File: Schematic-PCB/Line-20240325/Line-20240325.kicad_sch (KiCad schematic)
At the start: 137 parts, among them J1 Conn_01x02_Pin, J2 Conn_01x04_Pin, J3 USB_C_Receptacle_USB2.0_16P, SW1 SW_Push, U33 ATmega2560-16A, U34 CH340E, Y1 16MHz

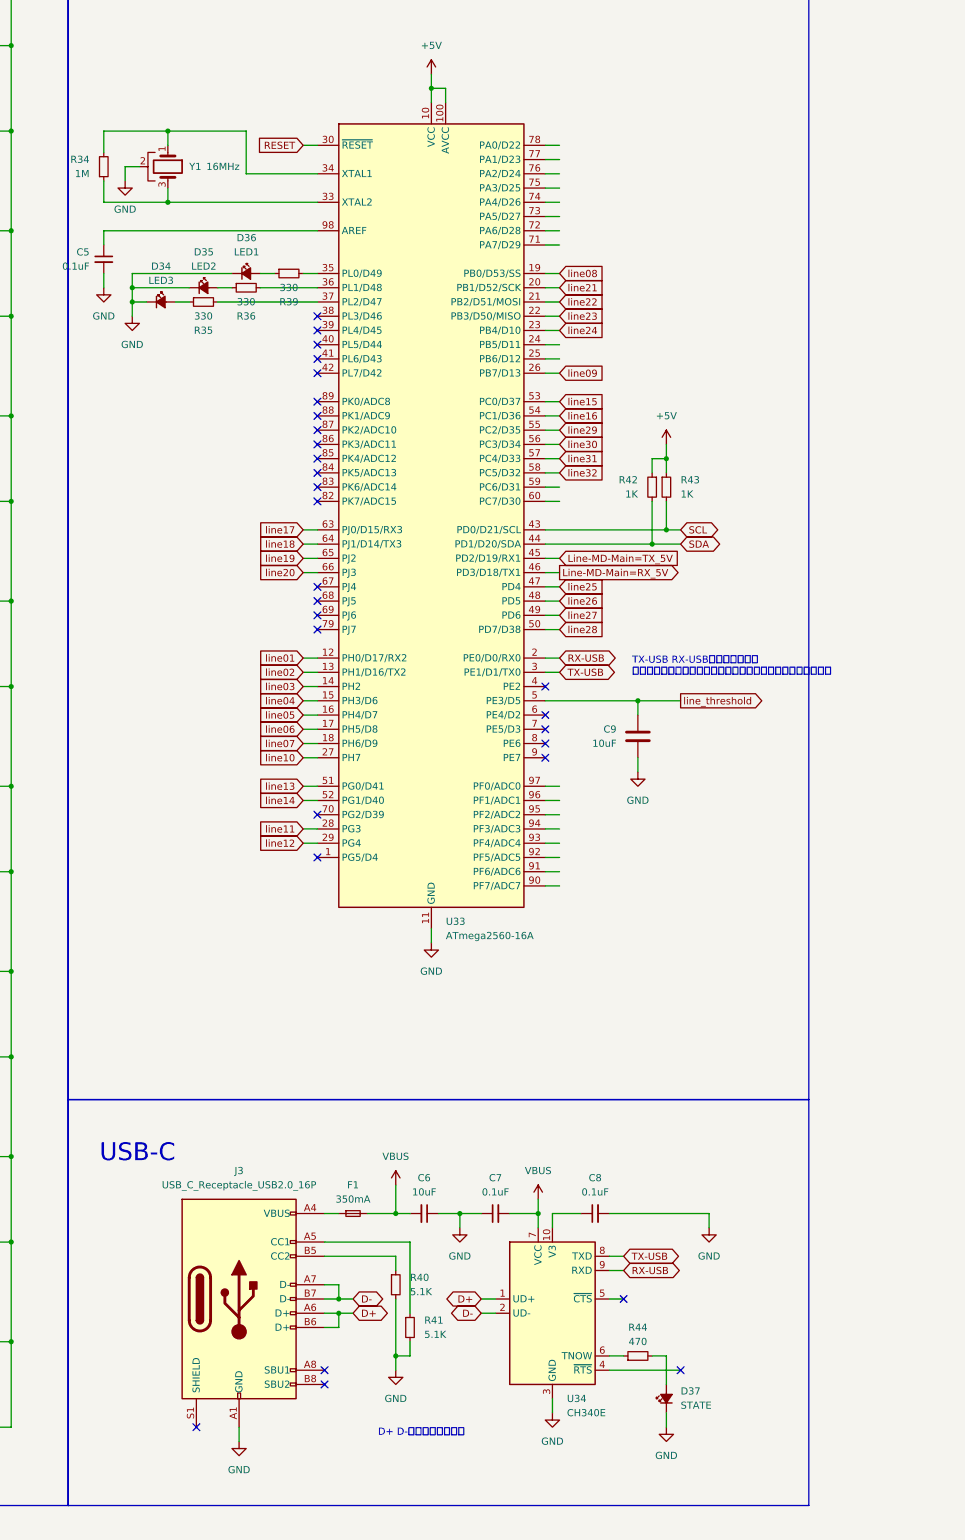
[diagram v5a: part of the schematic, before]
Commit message: ラインセンサ基板の回路図を見直した
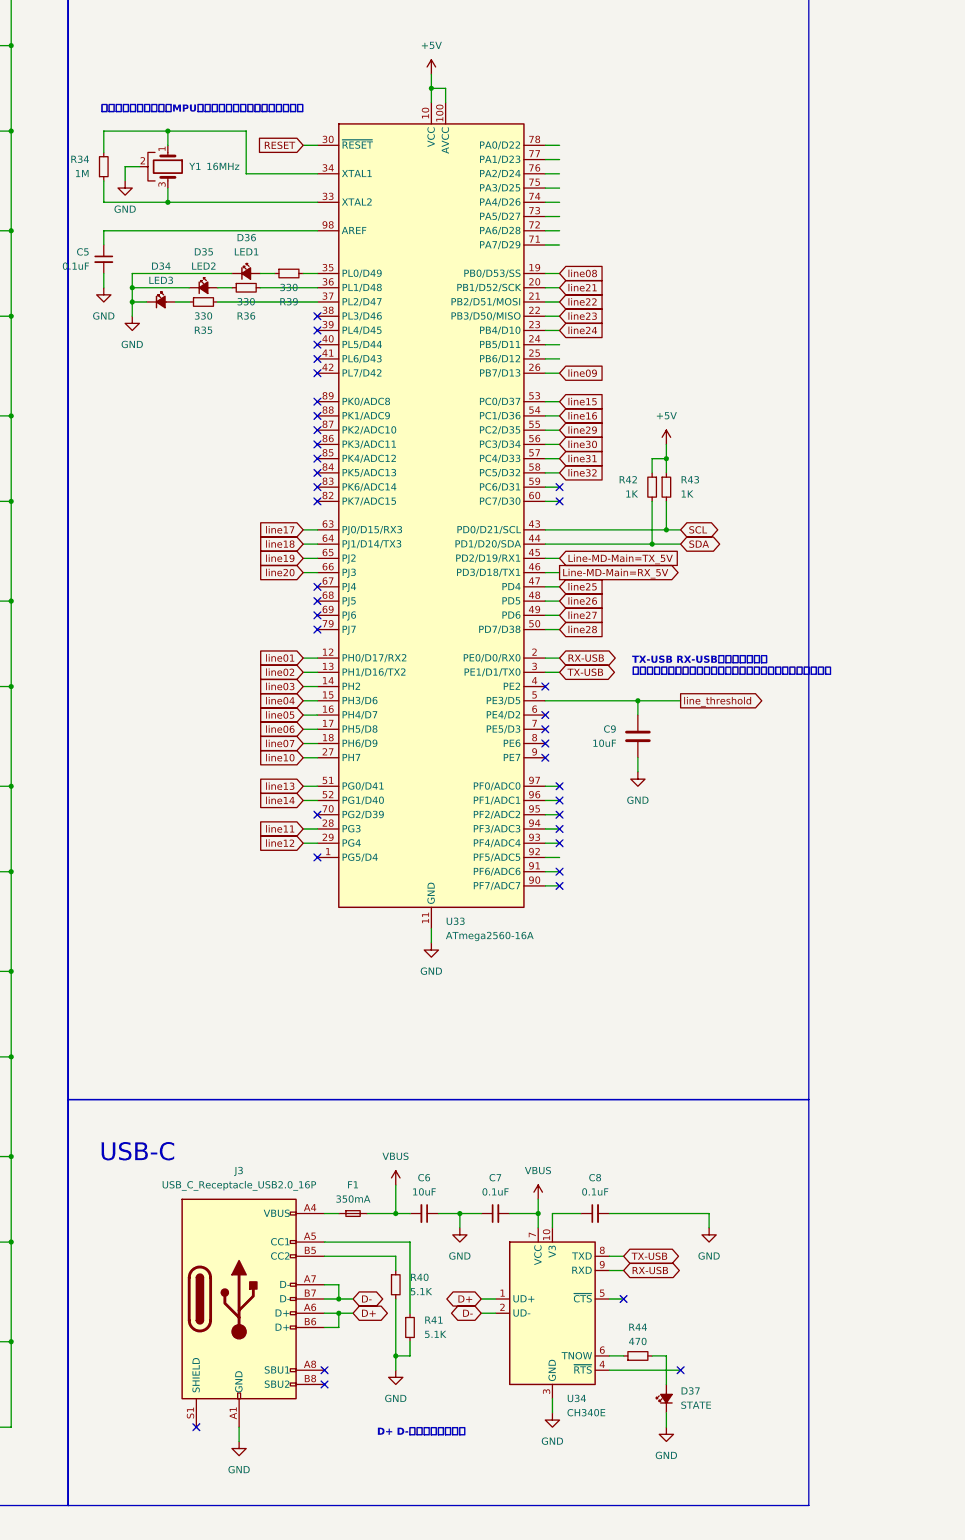
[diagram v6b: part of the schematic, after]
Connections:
- no-connect marks 29 -> 38
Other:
- note added: "クロックの発振子からMPUのピンまでの距離は同距離にする"
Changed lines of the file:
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@@
 	)
 	(no_connect
+		(at 256.54 180.34)
+	)
+	(no_connect
 		(at 213.36 114.3)
 	)
@@
 	)
 	(no_connect
+		(at 256.54 187.96)
+	)
+	(no_connect
+		(at 256.54 170.18)
+	)
+	(no_connect
 		(at 213.36 104.14)
 	)
 	(no_connect
+		(at 256.54 172.72)
+	)
+	(no_connect
 		(at 254 162.56)
 	)
 	(no_connect
+		(at 256.54 119.38)
+	)
+	(no_connect
 		(at 213.36 101.6)
 	)
@@
 	)
 	(no_connect
+		(at 256.54 185.42)
+	)
+	(no_connect
 		(at 213.36 116.84)
 	)
@@
 	)
 	(no_connect
+		(at 256.54 175.26)
+	)
+	(no_connect
 		(at 213.36 88.9)
 	)
@@
 	)
 	(no_connect
+		(at 256.54 177.8)
+	)
+	(no_connect
 		(at 213.36 91.44)
 	)
@@
 		(at 213.36 137.16)
 	)
+	(no_connect
+		(at 256.54 116.84)
+	)
 	(wire
 		(pts
@@
 		(effects
 			(font
+				(face "游ゴシック")
 				(size 1.27 1.27)
+				(thickness 0.254)
+				(bold yes)
 			)
 			(justify left)
@@
 		)
 	)
+	(text "クロックの発振子からMPUのピンまでの距離は同距離にする"
+		(exclude_from_sim no)
+		(at 174.752 49.53 0)
+		(effects
+			(font
+				(face "游ゴシック")
+				(size 1.27 1.27)
+				(thickness 0.254)
+				(bold yes)
+			)
+			(justify left)
+		)
+	)
 	(text "D+ D-間は短く配線する\n"
 		(exclude_from_sim no)
@@
 		(effects
 			(font
+				(face "游ゴシック")
 				(size 1.27 1.27)
+				(thickness 0.254)
+				(bold yes)
 			)
 		)

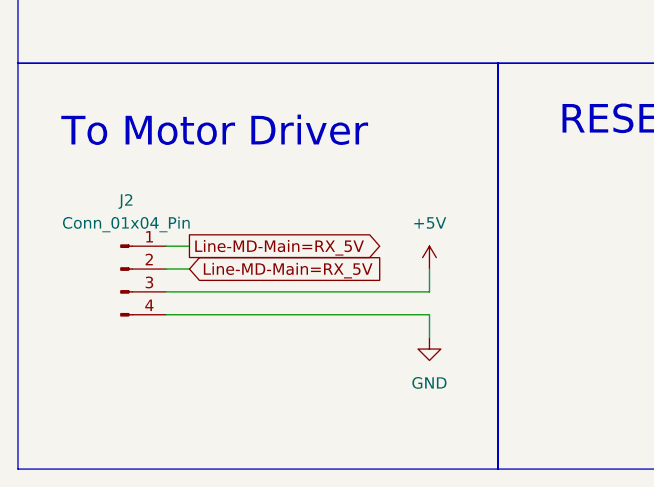
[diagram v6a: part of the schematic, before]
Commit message: ライン基板のPCBを更新した
・SDA・SCLが回路的にどこにも繋がれていない
・USB-Cのコネクタのフットプリントが不明
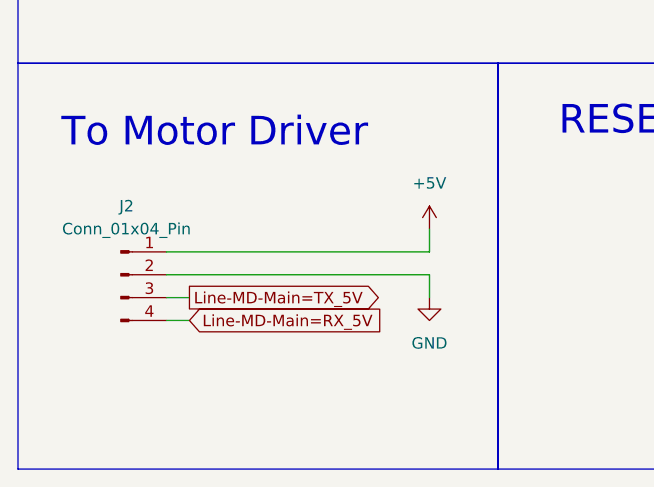
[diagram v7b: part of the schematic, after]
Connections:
- net +5V: now also J2.1 (Pin_1); no longer J2.3 (Pin_3)
- net GND: now also J2.2 (Pin_2); no longer J2.4 (Pin_4)
- net Line-MD-Main=RX_5V: now also J2.4 (Pin_4); no longer J2.1 (Pin_1), J2.2 (Pin_2)
- net Line-MD-Main=TX_5V: now also J2.3 (Pin_3)
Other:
- moved on the sheet: J2
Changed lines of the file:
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@@
 	(wire
 		(pts
-			(xy 29.21 363.855) (xy 31.75 363.855)
+			(xy 29.21 364.49) (xy 58.42 364.49)
 		)
 		(stroke
@@
 	(wire
 		(pts
-			(xy 29.21 366.395) (xy 31.75 366.395)
+			(xy 29.21 367.03) (xy 58.42 367.03)
 		)
 		(stroke
@@
 	(wire
 		(pts
+			(xy 29.21 372.11) (xy 31.75 372.11)
+		)
+		(stroke
+			(width 0)
+			(type default)
+		)
+	)
+	(wire
+		(pts
 			(xy 35.56 57.15) (xy 35.56 63.5)
 		)
@@
 	(wire
 		(pts
-			(xy 58.42 366.395) (xy 58.42 368.935)
+			(xy 58.42 361.95) (xy 58.42 364.49)
 		)
 		(stroke
@@
 	(wire
 		(pts
-			(xy 29.21 371.475) (xy 58.42 371.475)
+			(xy 29.21 369.57) (xy 31.75 369.57)
 		)
 		(stroke
@@
 	(wire
 		(pts
-			(xy 29.21 368.935) (xy 58.42 368.935)
-		)
-		(stroke
-			(width 0)
-			(type default)
-		)
-	)
-	(wire
-		(pts
 			(xy 35.56 44.45) (xy 35.56 50.8)
 		)
@@
 	(wire
 		(pts
-			(xy 58.42 371.475) (xy 58.42 374.015)
+			(xy 58.42 367.03) (xy 58.42 369.57)
 		)
 		(stroke
@@
 		)
 	)
-	(global_label "Line-MD-Main=RX_5V"
-		(shape output)
-		(at 31.75 363.855 0)
-		(fields_autoplaced yes)
-		(effects
-			(font
-				(size 1.27 1.27)
-			)
-			(justify left)
-		)
-		(property "Intersheetrefs" "${INTERSHEET_REFS}"
-			(at 56.1437 363.855 0)
-			(effects
-				(font
-					(size 1.27 1.27)
-				)
-				(justify left)
-				(hide yes)
-			)
-		)
-	)
 	(global_label "line_threshold"
 		(shape input)
@@
 		)
 	)
-	(global_label "Line-MD-Main=RX_5V"
-		(shape input)
-		(at 31.75 366.395 0)
-		(fields_autoplaced yes)
-		(effects
-			(font
-				(size 1.27 1.27)
-			)
-			(justify left)
-		)
-		(property "Intersheetrefs" "${INTERSHEET_REFS}"
-			(at 56.1437 366.395 0)
-			(effects
-				(font
-					(size 1.27 1.27)
-				)
-				(justify left)
-				(hide yes)
-			)
-		)
-	)
 	(global_label "line02"
 		(shape output)
@@
 		)
 	)
+	(global_label "Line-MD-Main=TX_5V"
+		(shape output)
+		(at 31.75 369.57 0)
+		(fields_autoplaced yes)
+		(effects
+			(font
+				(size 1.27 1.27)
+			)
+			(justify left)
+		)
+		(property "Intersheetrefs" "${INTERSHEET_REFS}"
+			(at 55.8413 369.57 0)
+			(effects
+				(font
+					(size 1.27 1.27)
+				)
+				(justify left)
+				(hide yes)
+			)
+		)
+	)
 	(global_label "line32"
 		(shape output)
@@
 		)
 	)
+	(global_label "Line-MD-Main=RX_5V"
+		(shape input)
+		(at 31.75 372.11 0)
+		(fields_autoplaced yes)
+		(effects
+			(font
+				(size 1.27 1.27)
+			)
+			(justify left)
+		)
+		(property "Intersheetrefs" "${INTERSHEET_REFS}"
+			(at 56.1437 372.11 0)
+			(effects
+				(font
+					(size 1.27 1.27)
+				)
+				(justify left)
+				(hide yes)
+			)
+		)
+	)
 	(global_label "line27"
 		(shape input)
@@
 	(symbol
 		(lib_id "power:+5V")
-		(at 58.42 366.395 0)
+		(at 58.42 361.95 0)
 		(unit 1)
 		(exclude_from_sim no)
@@
 		(fields_autoplaced yes)
 		(property "Reference" "#PWR026"
-			(at 58.42 370.205 0)
+			(at 58.42 365.76 0)
 			(effects
 				(font
@@
 		)
 		(property "Value" "+5V"
-			(at 58.42 361.315 0)
+			(at 58.42 356.87 0)
 			(effects
 				(font
@@
 		)
 		(property "Footprint" ""
-			(at 58.42 366.395 0)
+			(at 58.42 361.95 0)
 			(effects
 				(font
@@
 		)
 		(property "Datasheet" ""
-			(at 58.42 366.395 0)
+			(at 58.42 361.95 0)
 			(effects
 				(font
@@
 		)
 		(property "Description" "Power symbol creates a global label with name \"+5V\""
-			(at 58.42 366.395 0)
+			(at 58.42 361.95 0)
 			(effects
 				(font
@@
 	(symbol
 		(lib_id "Connector:Conn_01x04_Pin")
-		(at 24.13 366.395 0)
+		(at 24.13 367.03 0)
 		(unit 1)
 		(exclude_from_sim no)
@@
 		(fields_autoplaced yes)
 		(property "Reference" "J2"
-			(at 24.765 358.775 0)
+			(at 24.765 359.41 0)
 			(effects
 				(font
@@
 		)
 		(property "Value" "Conn_01x04_Pin"
-			(at 24.765 361.315 0)
+			(at 24.765 361.95 0)
 			(effects
 				(font
@@
 		)
 		(property "Footprint" "Connector_JST:JST_XH_S4B-XH-A-1_1x04_P2.50mm_Horizontal"
-			(at 24.13 366.395 0)
+			(at 24.13 367.03 0)
 			(effects
 				(font
@@
 		)
 		(property "Datasheet" "~"
-			(at 24.13 366.395 0)
+			(at 24.13 367.03 0)
 			(effects
 				(font
@@
 		)
 		(property "Description" "Generic connector, single row, 01x04, script generated"
-			(at 24.13 366.395 0)
+			(at 24.13 367.03 0)
 			(effects
 				(font
@@
 	(symbol
 		(lib_id "power:GND")
-		(at 58.42 374.015 0)
+		(at 58.42 369.57 0)
 		(unit 1)
 		(exclude_from_sim no)
@@
 		(fields_autoplaced yes)
 		(property "Reference" "#PWR027"
-			(at 58.42 380.365 0)
+			(at 58.42 375.92 0)
 			(effects
 				(font
@@
 		)
 		(property "Value" "GND"
-			(at 58.42 379.095 0)
+			(at 58.42 374.65 0)
 			(effects
 				(font
@@
 		)
 		(property "Footprint" ""
-			(at 58.42 374.015 0)
+			(at 58.42 369.57 0)
 			(effects
 				(font
@@
 		)
 		(property "Datasheet" ""
-			(at 58.42 374.015 0)
+			(at 58.42 369.57 0)
 			(effects
 				(font
@@
 		)
 		(property "Description" "Power symbol creates a global label with name \"GND\" , ground"
-			(at 58.42 374.015 0)
+			(at 58.42 369.57 0)
 			(effects
 				(font

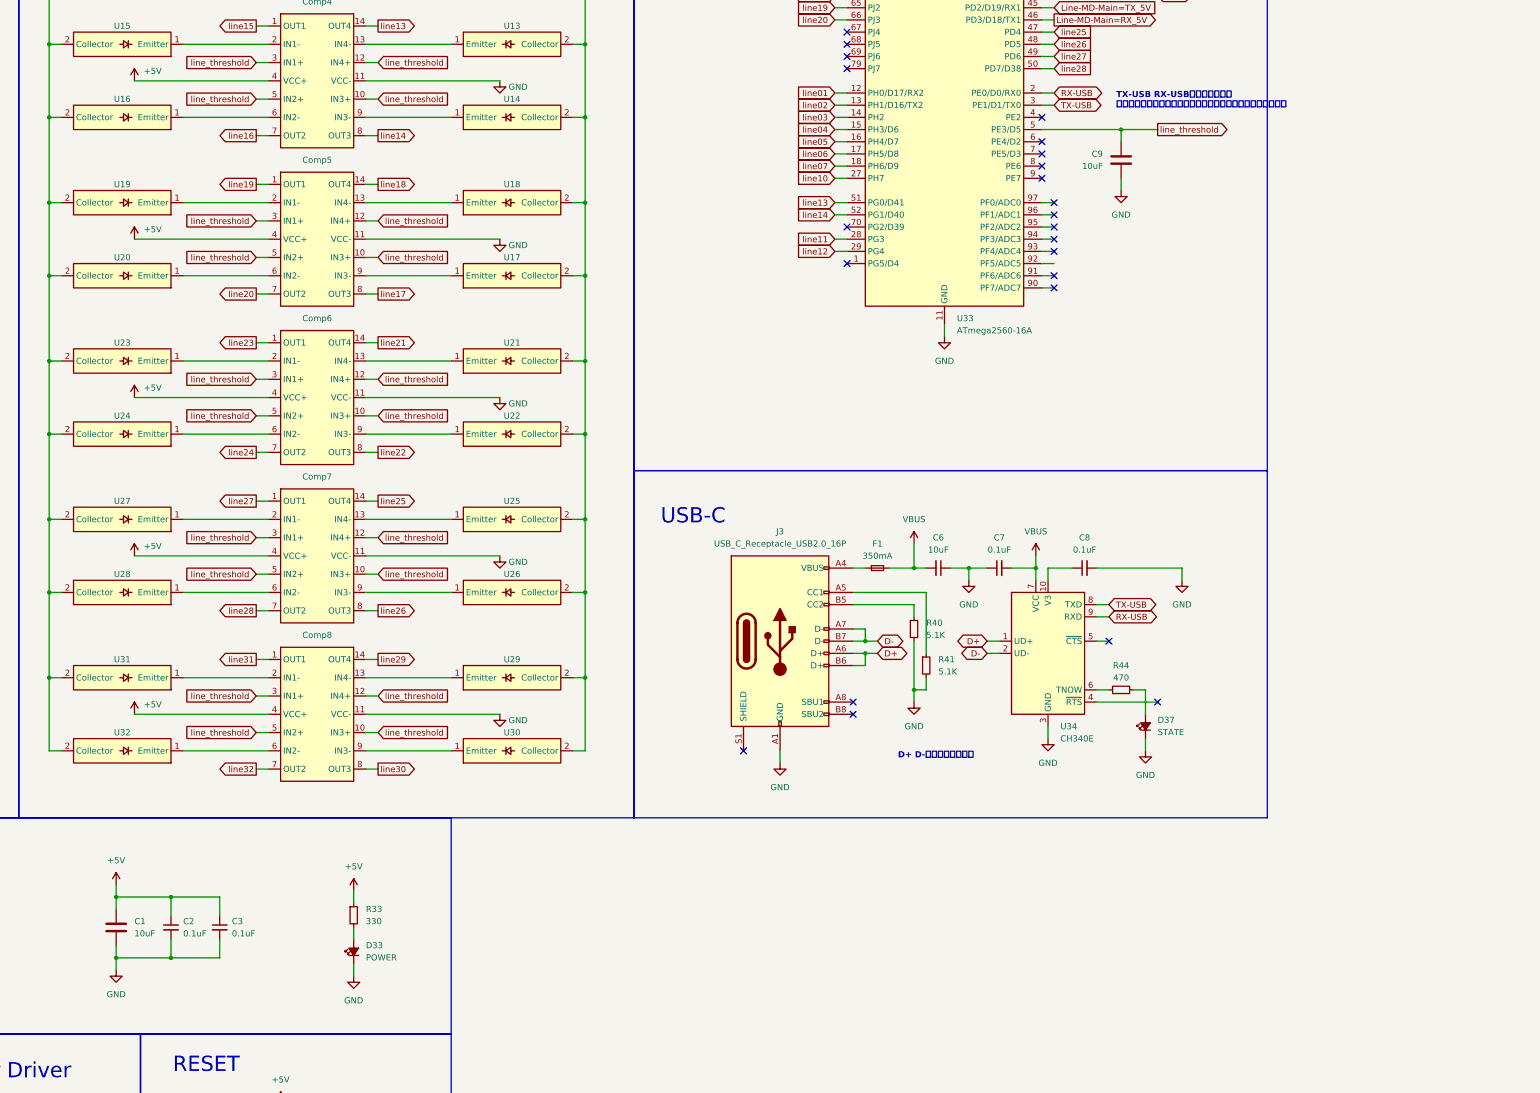
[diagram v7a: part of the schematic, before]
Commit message: ラインセンサ基板の回路図を少しだけいじった
UARTUSBのノイズ除去用の抵抗を追加してみた（ジャンパで切り替え可能）
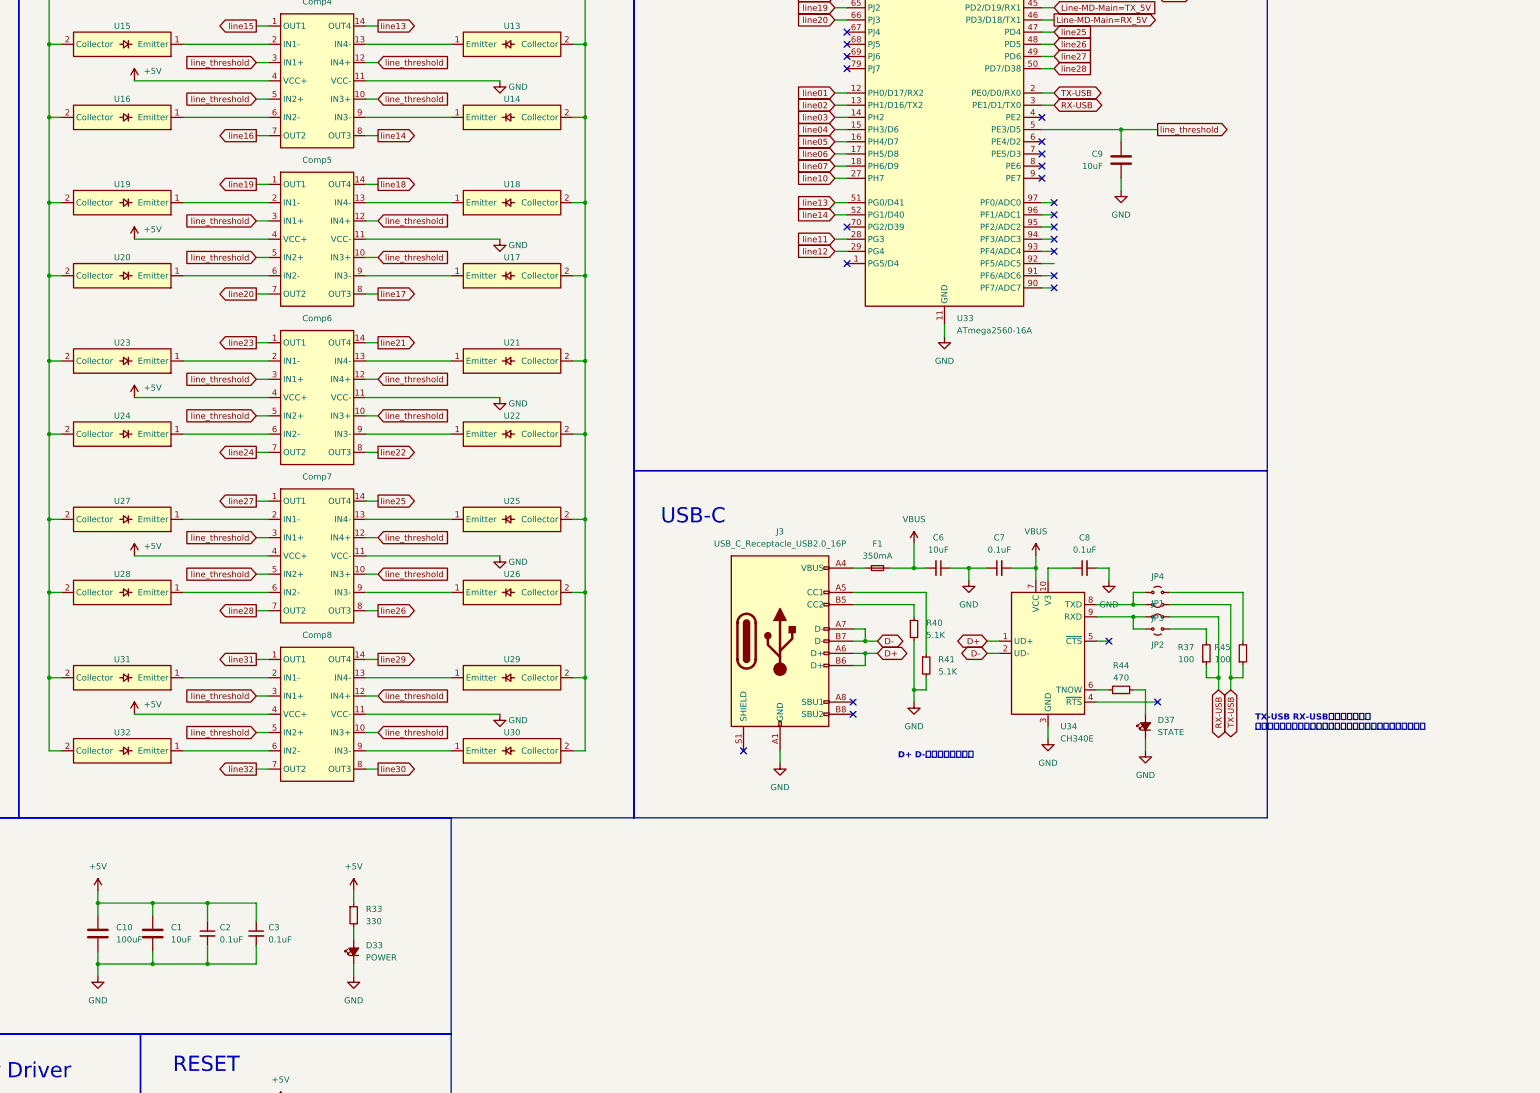
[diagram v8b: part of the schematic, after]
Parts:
- added C10: 100uF, Capacitor_SMD:C_0603_1608Metric, symbol Device:C
- added JP1, JP3: Jumper_2_Small_Bridged, symbol Jumper:Jumper_2_Small_Bridged
- added JP2, JP4: Jumper_2_Small_Open, symbol Jumper:Jumper_2_Small_Open
- added R37, R45: 100, symbol Device:R_Small
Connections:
- net +5V: now also C10.1
- net GND: now also C10.2
- net RX-USB: now also U33.3 (PE1/D1/TX0), JP1.2 (B), R37.1; no longer U33.2 (PE0/D0/RX0), U34.9 (RXD)
- net TX-USB: now also U33.2 (PE0/D0/RX0), JP3.2 (B), R45.1; no longer U33.3 (PE1/D1/TX0), U34.8 (TXD)
- new net: JP2.1 (A), R37.2
- new net: JP4.1 (A), R45.2
- new net: JP1.1 (A), JP2.2 (B), U34.9 (RXD)
- new net: JP3.1 (A), JP4.2 (B), U34.8 (TXD)
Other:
- moved on the sheet: C1, C2, C3
